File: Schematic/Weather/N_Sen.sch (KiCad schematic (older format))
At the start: 23 parts, among them J2 4_Way_Wire, J3 4_Way_Wire, Q1 BSS138, Q2 AO3401, Q3 AO3401, U5 LM321

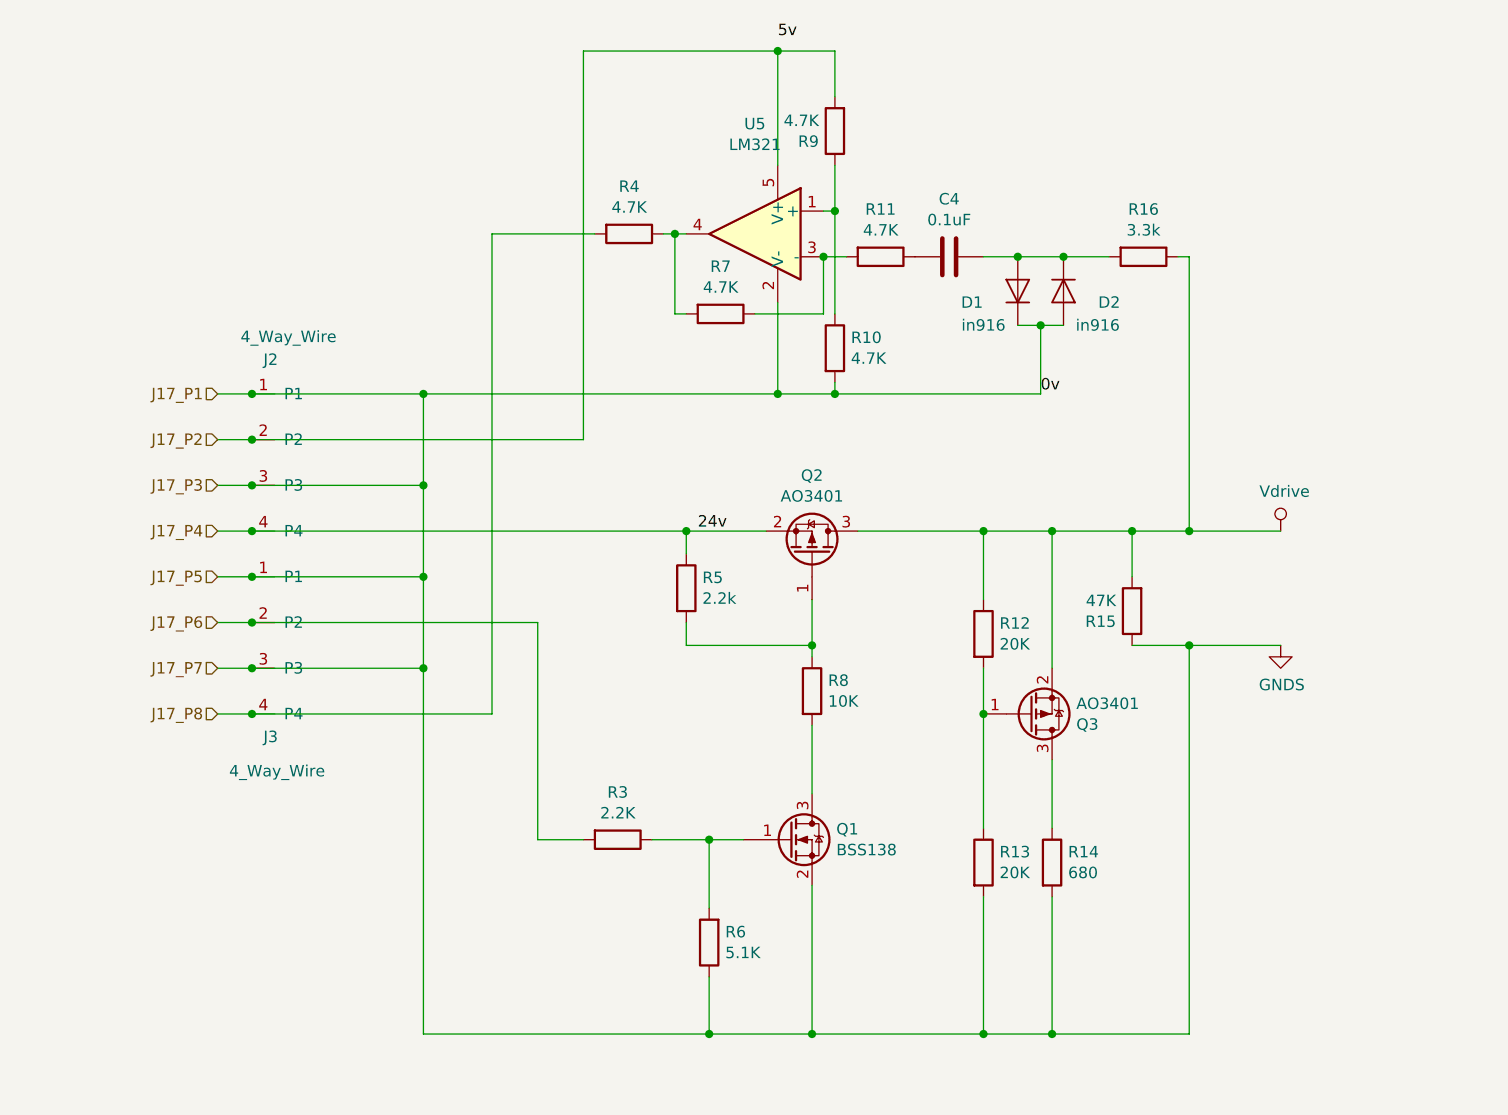
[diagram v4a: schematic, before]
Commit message: Borad layout 2x for Tx Rx
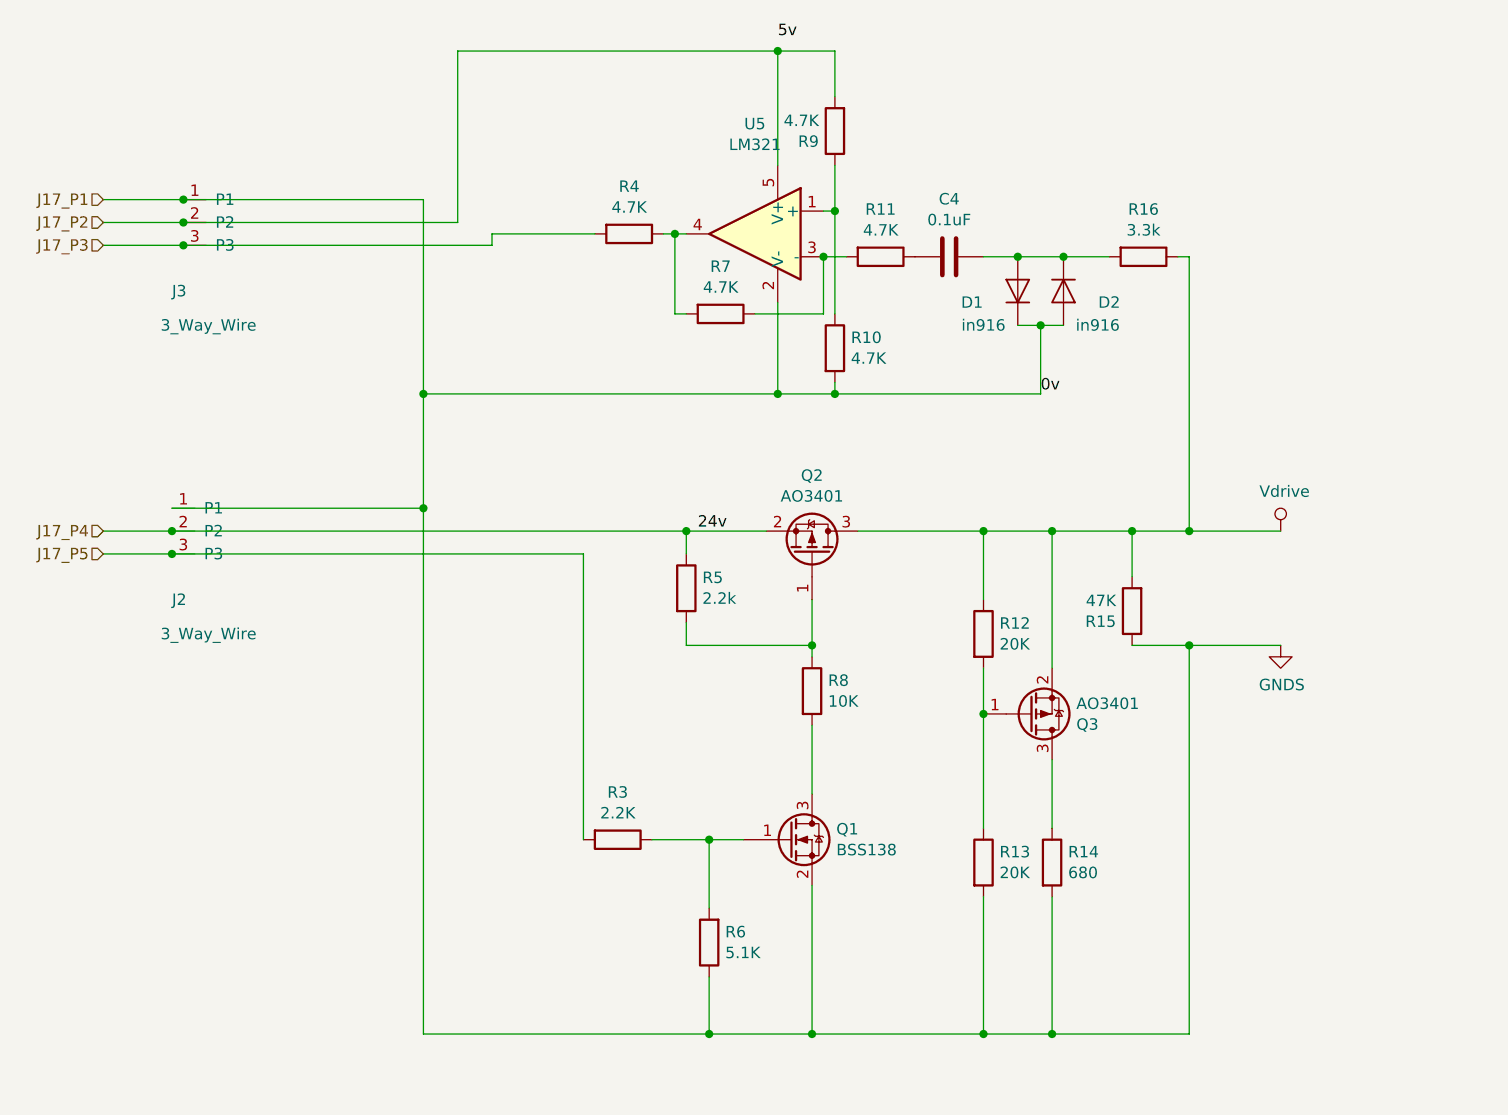
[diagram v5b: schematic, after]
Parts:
- removed J2, J3: 4_Way_Wire, Connector_PinHeader_2.54mm:PinHeader_1x04_P2.54mm_Vertical, symbol MyComponents:4_Way_Wire
- added J2, J3: 3_Way_Wire, Connector_PinHeader_2.54mm:PinHeader_1x03_P2.54mm_Vertical, symbol MyComponents:3_Way_Wire
- D1: footprint Diode_THT:D_DO-35_SOD27_P7.62mm_Horizontal -> Diode_THT:D_DO-35_SOD27_P2.54mm_Vertical_KathodeUp
- D2: footprint Diode_THT:D_DO-35_SOD27_P7.62mm_Horizontal -> Diode_THT:D_DO-35_SOD27_P2.54mm_Vertical_AnodeUp
- R10, R11, R12, R13, R14, R15, R16, R3, R4, R5, R6, R7, R8, R9: footprint Resistor_THT:R_Axial_DIN0207_L6.3mm_D2.5mm_P7.62mm_Horizontal -> Resistor_THT:R_Axial_DIN0204_L3.6mm_D1.6mm_P2.54mm_Vertical
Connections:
- net GNDS: now also J2.1 (P1), J3.1 (P1)
- net J17_P2: now also J3.2 (P2)
- net J17_P4: now also J2.2 (P2)
- net J17_P6 renamed J17_P5
- net J17_P5: now also J2.3 (P3)
- net J17_P8 renamed J17_P3
- net J17_P3: now also J3.3 (P3)
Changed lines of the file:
@@
 Comment4 ""
 $EndDescr
-Text HLabel 3700 2850 0    50   Input ~ 0
+Text HLabel 3200 2000 0    50   Input ~ 0
 J17_P1
-Text HLabel 3700 3050 0    50   Input ~ 0
+Text HLabel 3200 2100 0    50   Input ~ 0
 J17_P2
-Text HLabel 3700 3250 0    50   Input ~ 0
+Text HLabel 3200 2200 0    50   Input ~ 0
 J17_P3
-Text HLabel 3700 3450 0    50   Input ~ 0
+Text HLabel 3200 3450 0    50   Input ~ 0
 J17_P4
-Text HLabel 3700 4050 0    50   Input ~ 0
-J17_P7
-Text HLabel 3700 4250 0    50   Input ~ 0
-J17_P8
 $Comp
 L Weather-rescue:AO3401-Transistor_FET Q2
@@
 F 0 "R3" V 5243 4800 50  0000 C CNN
 F 1 "2.2K" V 5334 4800 50  0000 C CNN
-F 2 "Resistor_THT:R_Axial_DIN0207_L6.3mm_D2.5mm_P7.62mm_Horizontal" V 5380 4800 50  0001 C CNN
+F 2 "Resistor_THT:R_Axial_DIN0204_L3.6mm_D1.6mm_P2.54mm_Vertical" V 5380 4800 50  0001 C CNN
 F 3 "~" H 5450 4800 50  0001 C CNN
 	1    5450 4800
@@
 F 0 "R6" H 5780 5204 50  0000 R CNN
 F 1 "5.1K" H 5780 5295 50  0000 R CNN
-F 2 "Resistor_THT:R_Axial_DIN0207_L6.3mm_D2.5mm_P7.62mm_Horizontal" V 5780 5250 50  0001 C CNN
+F 2 "Resistor_THT:R_Axial_DIN0204_L3.6mm_D1.6mm_P2.54mm_Vertical" V 5780 5250 50  0001 C CNN
 F 3 "~" H 5850 5250 50  0001 C CNN
 	1    5850 5250
@@
 F 0 "R14" H 7420 4946 50  0000 L CNN
 F 1 "680" H 7420 4855 50  0000 L CNN
-F 2 "Resistor_THT:R_Axial_DIN0207_L6.3mm_D2.5mm_P7.62mm_Horizontal" V 7280 4900 50  0001 C CNN
+F 2 "Resistor_THT:R_Axial_DIN0204_L3.6mm_D1.6mm_P2.54mm_Vertical" V 7280 4900 50  0001 C CNN
 F 3 "~" H 7350 4900 50  0001 C CNN
 	1    7350 4900
@@
 F 0 "R12" H 7120 3946 50  0000 L CNN
 F 1 "20K" H 7120 3855 50  0000 L CNN
-F 2 "Resistor_THT:R_Axial_DIN0207_L6.3mm_D2.5mm_P7.62mm_Horizontal" V 6980 3900 50  0001 C CNN
+F 2 "Resistor_THT:R_Axial_DIN0204_L3.6mm_D1.6mm_P2.54mm_Vertical" V 6980 3900 50  0001 C CNN
 F 3 "~" H 7050 3900 50  0001 C CNN
 	1    7050 3900
@@
 F 0 "R8" H 6370 4196 50  0000 L CNN
 F 1 "10K" H 6370 4105 50  0000 L CNN
-F 2 "Resistor_THT:R_Axial_DIN0207_L6.3mm_D2.5mm_P7.62mm_Horizontal" V 6230 4150 50  0001 C CNN
+F 2 "Resistor_THT:R_Axial_DIN0204_L3.6mm_D1.6mm_P2.54mm_Vertical" V 6230 4150 50  0001 C CNN
 F 3 "~" H 6300 4150 50  0001 C CNN
 	1    6300 4150
@@
 F 0 "R5" H 5820 3746 50  0000 L CNN
 F 1 "2.2k" H 5820 3655 50  0000 L CNN
-F 2 "Resistor_THT:R_Axial_DIN0207_L6.3mm_D2.5mm_P7.62mm_Horizontal" V 5680 3700 50  0001 C CNN
+F 2 "Resistor_THT:R_Axial_DIN0204_L3.6mm_D1.6mm_P2.54mm_Vertical" V 5680 3700 50  0001 C CNN
 F 3 "~" H 5750 3700 50  0001 C CNN
 	1    5750 3700
@@
 F 0 "R9" H 6470 1746 50  0000 L CNN
 F 1 "4.7K" H 6470 1655 50  0000 L CNN
-F 2 "Resistor_THT:R_Axial_DIN0207_L6.3mm_D2.5mm_P7.62mm_Horizontal" V 6330 1700 50  0001 C CNN
+F 2 "Resistor_THT:R_Axial_DIN0204_L3.6mm_D1.6mm_P2.54mm_Vertical" V 6330 1700 50  0001 C CNN
 F 3 "~" H 6400 1700 50  0001 C CNN
 	1    6400 1700
@@
 F 0 "D2" V 7450 2600 50  0000 C CNN
 F 1 "in916" V 7550 2550 50  0000 C CNN
-F 2 "Diode_THT:D_DO-35_SOD27_P7.62mm_Horizontal" H 7400 2400 50  0001 C CNN
+F 2 "Diode_THT:D_DO-35_SOD27_P2.54mm_Vertical_AnodeUp" H 7400 2400 50  0001 C CNN
 F 3 "~" H 7400 2400 50  0001 C CNN
 	1    7400 2400
@@
 F 0 "D1" V 7150 2600 50  0000 C CNN
 F 1 "in916" V 7050 2550 50  0000 C CNN
-F 2 "Diode_THT:D_DO-35_SOD27_P7.62mm_Horizontal" H 7200 2400 50  0001 C CNN
+F 2 "Diode_THT:D_DO-35_SOD27_P2.54mm_Vertical_KathodeUp" H 7200 2400 50  0001 C CNN
 F 3 "~" H 7200 2400 50  0001 C CNN
 	1    7200 2400
@@
 F 0 "R4" V 5293 2150 50  0000 C CNN
 F 1 "4.7K" V 5384 2150 50  0000 C CNN
-F 2 "Resistor_THT:R_Axial_DIN0207_L6.3mm_D2.5mm_P7.62mm_Horizontal" V 5430 2150 50  0001 C CNN
+F 2 "Resistor_THT:R_Axial_DIN0204_L3.6mm_D1.6mm_P2.54mm_Vertical" V 5430 2150 50  0001 C CNN
 F 3 "~" H 5500 2150 50  0001 C CNN
 	1    5500 2150
@@
 F 0 "R13" H 7120 4946 50  0000 L CNN
 F 1 "20K" H 7120 4855 50  0000 L CNN
-F 2 "Resistor_THT:R_Axial_DIN0207_L6.3mm_D2.5mm_P7.62mm_Horizontal" V 6980 4900 50  0001 C CNN
+F 2 "Resistor_THT:R_Axial_DIN0204_L3.6mm_D1.6mm_P2.54mm_Vertical" V 6980 4900 50  0001 C CNN
 F 3 "~" H 7050 4900 50  0001 C CNN
 	1    7050 4900
@@
 F 0 "R16" V 7543 2250 50  0000 C CNN
 F 1 "3.3k" V 7634 2250 50  0000 C CNN
-F 2 "Resistor_THT:R_Axial_DIN0207_L6.3mm_D2.5mm_P7.62mm_Horizontal" V 7680 2250 50  0001 C CNN
+F 2 "Resistor_THT:R_Axial_DIN0204_L3.6mm_D1.6mm_P2.54mm_Vertical" V 7680 2250 50  0001 C CNN
 F 3 "~" H 7750 2250 50  0001 C CNN
 	1    7750 2250
@@
 F 0 "R10" H 6470 2696 50  0000 L CNN
 F 1 "4.7K" H 6470 2605 50  0000 L CNN
-F 2 "Resistor_THT:R_Axial_DIN0207_L6.3mm_D2.5mm_P7.62mm_Horizontal" V 6330 2650 50  0001 C CNN
+F 2 "Resistor_THT:R_Axial_DIN0204_L3.6mm_D1.6mm_P2.54mm_Vertical" V 6330 2650 50  0001 C CNN
 F 3 "~" H 6400 2650 50  0001 C CNN
 	1    6400 2650
@@
 Connection ~ 7950 3950
 Wire Wire Line
-	3850 4050 4600 4050
-Wire Wire Line
-	4600 4050 4600 5650
-Wire Wire Line
 	4600 5650 5850 5650
 Connection ~ 5850 5650
 Wire Wire Line
-	3850 3650 4600 3650
-Wire Wire Line
-	4600 3650 4600 4050
-Connection ~ 4600 4050
-Wire Wire Line
-	3850 3250 4600 3250
-Wire Wire Line
-	4600 3250 4600 3650
-Connection ~ 4600 3650
-Wire Wire Line
-	4600 2850 4600 3250
-Connection ~ 4600 3250
-Wire Wire Line
-	3850 3850 5100 3850
-Wire Wire Line
-	5100 3850 5100 4800
-Wire Wire Line
-	5100 4800 5300 4800
-Wire Wire Line
-	3850 4250 4900 4250
-Wire Wire Line
-	4900 4250 4900 2150
-Wire Wire Line
 	6150 2450 6150 2850
 Wire Wire Line
 	6150 2850 4600 2850
-Wire Wire Line
-	3850 3050 5300 3050
-Wire Wire Line
-	5300 3050 5300 1350
 Wire Wire Line
 	6150 2850 6400 2850
@@
 Wire Wire Line
 	4900 2150 5350 2150
-Wire Wire Line
-	5300 1350 6150 1350
-Wire Wire Line
-	3850 2850 4600 2850
-Connection ~ 4600 2850
 Text Label 5800 3450 0    50   ~ 0
 24v
@@
 F 0 "R11" V 6393 2250 50  0000 C CNN
 F 1 "4.7K" V 6484 2250 50  0000 C CNN
-F 2 "Resistor_THT:R_Axial_DIN0207_L6.3mm_D2.5mm_P7.62mm_Horizontal" V 6530 2250 50  0001 C CNN
+F 2 "Resistor_THT:R_Axial_DIN0204_L3.6mm_D1.6mm_P2.54mm_Vertical" V 6530 2250 50  0001 C CNN
 F 3 "~" H 6600 2250 50  0001 C CNN
 	1    6600 2250
@@
 F 0 "R7" V 5693 2500 50  0000 C CNN
 F 1 "4.7K" V 5784 2500 50  0000 C CNN
-F 2 "Resistor_THT:R_Axial_DIN0207_L6.3mm_D2.5mm_P7.62mm_Horizontal" V 5830 2500 50  0001 C CNN
+F 2 "Resistor_THT:R_Axial_DIN0204_L3.6mm_D1.6mm_P2.54mm_Vertical" V 5830 2500 50  0001 C CNN
 F 3 "~" H 5900 2500 50  0001 C CNN
 	1    5900 2500
@@
 	6350 2500 6350 2250
 Connection ~ 6350 2250
-Wire Wire Line
-	3850 2850 3700 2850
-Connection ~ 3850 2850
-Wire Wire Line
-	3850 3050 3700 3050
-Connection ~ 3850 3050
-Wire Wire Line
-	3850 3250 3700 3250
-Connection ~ 3850 3250
-Wire Wire Line
-	3850 3650 3700 3650
-Connection ~ 3850 3650
-Wire Wire Line
-	3850 3850 3700 3850
-Connection ~ 3850 3850
-Wire Wire Line
-	3850 4050 3700 4050
-Connection ~ 3850 4050
-Wire Wire Line
-	3700 4250 3850 4250
-Connection ~ 3850 4250
-Text HLabel 3700 3850 0    50   Input ~ 0
-J17_P6
-Text HLabel 3700 3650 0    50   Input ~ 0
+Text HLabel 3200 3550 0    50   Input ~ 0
 J17_P5
-$Comp
-L MyComponents:4_Way_Wire J3
-U 1 1 5C97DFDF
-P 3950 3650
-F 0 "J3" H 3900 2950 50  0000 L CNN
-F 1 "4_Way_Wire" H 3750 2800 50  0000 L CNN
-F 2 "Connector_PinHeader_2.54mm:PinHeader_1x04_P2.54mm_Vertical" H 3850 3700 50  0001 C CNN
-F 3 "" H 3850 3700 50  0001 C CNN
-	1    3950 3650
-	1    0    0    -1
-$EndComp
-$Comp
-L MyComponents:4_Way_Wire J2
-U 1 1 5C97CF3A
-P 3950 2850
-F 0 "J2" H 3900 3000 50  0000 L CNN
-F 1 "4_Way_Wire" H 3800 3100 50  0000 L CNN
-F 2 "Connector_PinHeader_2.54mm:PinHeader_1x04_P2.54mm_Vertical" H 3850 2900 50  0001 C CNN
-F 3 "" H 3850 2900 50  0001 C CNN
-	1    3950 2850
-	1    0    0    -1
-$EndComp
 Wire Wire Line
 	5750 3850 5750 3950
 Wire Wire Line
 	6300 3750 6300 3950
-Wire Wire Line
-	3700 3450 3850 3450
-Connection ~ 5750 3450
-Connection ~ 3850 3450
-Wire Wire Line
-	3850 3450 5750 3450
-$Comp
-L power:GNDS #PWR0101
+$Comp
+L power:GNDS #PWR03
 U 1 1 5CFCB28B
 P 8350 3950
-F 0 "#PWR0101" H 8350 3700 50  0001 C CNN
+F 0 "#PWR03" H 8350 3700 50  0001 C CNN
 F 1 "GNDS" H 8355 3777 50  0000 C CNN
 F 2 "" H 8350 3950 50  0001 C CNN
@@
 F 0 "R15" H 7770 3846 50  0000 L CNN
 F 1 "47K" H 7770 3755 50  0000 L CNN
-F 2 "Resistor_THT:R_Axial_DIN0207_L6.3mm_D2.5mm_P7.62mm_Horizontal" V 7630 3800 50  0001 C CNN
+F 2 "Resistor_THT:R_Axial_DIN0204_L3.6mm_D1.6mm_P2.54mm_Vertical" V 7630 3800 50  0001 C CNN
 F 3 "~" H 7700 3800 50  0001 C CNN
 	1    7700 3800
@@
 $EndComp
 Connection ~ 7950 3450
+Wire Wire Line
+	4600 2850 4600 3350
+Wire Wire Line
+	4750 1350 6150 1350
+$Comp
+L MyComponents:3_Way_Wire J3
+U 1 1 5C9F0115
+P 3650 2000
+F 0 "J3" H 3500 1600 50  0000 L CNN
+F 1 "3_Way_Wire" H 3450 1450 50  0000 L CNN
+F 2 "Connector_PinHeader_2.54mm:PinHeader_1x03_P2.54mm_Vertical" H 3650 2000 50  0001 C CNN
+F 3 "" H 3650 2000 50  0001 C CNN
+	1    3650 2000
+	1    0    0    -1
+$EndComp
+Wire Wire Line
+	4600 2000 4600 2850
+Wire Wire Line
+	3200 2000 3550 2000
+Connection ~ 3550 2000
+Wire Wire Line
+	3550 2000 4600 2000
+Connection ~ 4600 2850
+$Comp
+L MyComponents:3_Way_Wire J2
+U 1 1 5C9F0A63
+P 3600 3350
+F 0 "J2" H 3500 2950 50  0000 L CNN
+F 1 "3_Way_Wire" H 3450 2800 50  0000 L CNN
+F 2 "Connector_PinHeader_2.54mm:PinHeader_1x03_P2.54mm_Vertical" H 3600 3350 50  0001 C CNN
+F 3 "" H 3600 3350 50  0001 C CNN
+	1    3600 3350
+	1    0    0    -1
+$EndComp
+Wire Wire Line
+	3500 3350 4600 3350
+Connection ~ 4600 3350
+Wire Wire Line
+	4600 3350 4600 5650
+Wire Wire Line
+	4750 2100 4750 1350
+Wire Wire Line
+	3200 2100 3550 2100
+Connection ~ 3550 2100
+Wire Wire Line
+	3550 2100 4750 2100
+Wire Wire Line
+	4900 2150 4900 2200
+Wire Wire Line
+	4900 2200 3550 2200
+Wire Wire Line
+	3200 2200 3550 2200
+Connection ~ 3550 2200
+Wire Wire Line
+	3200 3550 3500 3550
+Wire Wire Line
+	3500 3550 5300 3550
+Wire Wire Line
+	5300 3550 5300 4800
+Connection ~ 3500 3550
+Wire Wire Line
+	3200 3450 3500 3450
+Wire Wire Line
+	3500 3450 5750 3450
+Connection ~ 3500 3450
+Connection ~ 5750 3450
 $EndSCHEMATC

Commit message: more board layouts
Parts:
- added H1, H2, H3, H4: MountingHole_Pad, Connector_Wire:SolderWirePad_1x01_Drill0.8mm, symbol Mechanical:MountingHole_Pad
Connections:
- net GNDS: no longer D1.1 (K), D2.2 (A), J2.1 (P1), J3.1 (P1), Q1.2 (S), R10.2, R13.2, R14.2, R15.1, R6.1, U5.2 (V-)
- net Vdrive: no longer names the net of Q2.3 (D), Q3.2 (S), R12.1, R15.2, R16.1
- net Vdrive: now also H1.1, H2.1
- new net J17_P1: D1.1 (K), D2.2 (A), H3.1, H4.1, J2.1 (P1), J3.1 (P1), Q1.2 (S), R10.2, R13.2, R14.2, R15.1, R6.1, U5.2 (V-)
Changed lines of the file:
@@
 $Descr A4 11693 8268
 encoding utf-8
-Sheet 10 10
+Sheet 9 11
 Title ""
 Date ""
@@
 Wire Wire Line
 	6350 2050 6400 2050
-Wire Wire Line
-	7950 3950 8350 3950
 Connection ~ 7950 3950
 Wire Wire Line
@@
 	6300 3750 6300 3950
 $Comp
-L power:GNDS #PWR03
+L power:GNDS #PWR02
 U 1 1 5CFCB28B
-P 8350 3950
-F 0 "#PWR03" H 8350 3700 50  0001 C CNN
-F 1 "GNDS" H 8355 3777 50  0000 C CNN
-F 2 "" H 8350 3950 50  0001 C CNN
-F 3 "" H 8350 3950 50  0001 C CNN
-	1    8350 3950
+P 6300 5700
+F 0 "#PWR02" H 6300 5450 50  0001 C CNN
+F 1 "GNDS" H 6305 5527 50  0000 C CNN
+F 2 "" H 6300 5700 50  0001 C CNN
+F 3 "" H 6300 5700 50  0001 C CNN
+	1    6300 5700
 	1    0    0    -1
 $EndComp
@@
 Wire Wire Line
 	7950 2250 7950 3450
-$Comp
-L power:Vdrive #PWR02
-U 1 1 5C99BC4B
-P 8350 3450
-F 0 "#PWR02" H 8150 3300 50  0001 C CNN
-F 1 "Vdrive" H 8367 3623 50  0000 C CNN
-F 2 "" H 8350 3450 50  0001 C CNN
-F 3 "" H 8350 3450 50  0001 C CNN
-	1    8350 3450
-	1    0    0    -1
-$EndComp
 Connection ~ 7950 3450
 Wire Wire Line
@@
 Connection ~ 3500 3450
 Connection ~ 5750 3450
+$Comp
+L Mechanical:MountingHole_Pad H1
+U 1 1 5CA34377
+P 8350 3350
+F 0 "H1" H 8450 3399 50  0000 L CNN
+F 1 "MountingHole_Pad" H 8450 3308 50  0000 L CNN
+F 2 "Connector_Wire:SolderWirePad_1x01_Drill0.8mm" H 8350 3350 50  0001 C CNN
+F 3 "~" H 8350 3350 50  0001 C CNN
+	1    8350 3350
+	1    0    0    -1
+$EndComp
+$Comp
+L Mechanical:MountingHole_Pad H3
+U 1 1 5CA34DBD
+P 8350 3850
+F 0 "H3" H 8450 3899 50  0000 L CNN
+F 1 "MountingHole_Pad" H 8450 3808 50  0000 L CNN
+F 2 "Connector_Wire:SolderWirePad_1x01_Drill0.8mm" H 8350 3850 50  0001 C CNN
+F 3 "~" H 8350 3850 50  0001 C CNN
+	1    8350 3850
+	1    0    0    -1
+$EndComp
+$Comp
+L Mechanical:MountingHole_Pad H2
+U 1 1 5CA4F9CF
+P 8350 3550
+F 0 "H2" H 8250 3507 50  0000 R CNN
+F 1 "MountingHole_Pad" H 8250 3598 50  0000 R CNN
+F 2 "Connector_Wire:SolderWirePad_1x01_Drill0.8mm" H 8350 3550 50  0001 C CNN
+F 3 "~" H 8350 3550 50  0001 C CNN
+	1    8350 3550
+	-1   0    0    1
+$EndComp
+Connection ~ 8350 3450
+$Comp
+L Mechanical:MountingHole_Pad H4
+U 1 1 5CA5112A
+P 8350 4050
+F 0 "H4" H 8250 4007 50  0000 R CNN
+F 1 "MountingHole_Pad" H 8250 4098 50  0000 R CNN
+F 2 "Connector_Wire:SolderWirePad_1x01_Drill0.8mm" H 8350 4050 50  0001 C CNN
+F 3 "~" H 8350 4050 50  0001 C CNN
+	1    8350 4050
+	-1   0    0    1
+$EndComp
+Connection ~ 8350 3950
+Wire Wire Line
+	7950 3950 8350 3950
 $EndSCHEMATC
